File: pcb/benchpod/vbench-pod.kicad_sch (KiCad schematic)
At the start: 117 parts, among them J1 PZ254V-12-22P, SW1 TS-1088-AR02016, SW2 TS-1088-AR02016, U1 ICE40UP5K-SG48ITR, U10 TCAN1044VDRBRQ1, U2 W25Q64JVSSIQ, U24 SN74LVC2G66DCUR, U28 SRV05-4.TCT, U4 ESP32-C3-MINI-1-N4, U5 STM32H563ZIT6, U7 APS6404L-3SQR-ZR, U8 TPS2116DRLR, X1 SX3M48.000B10F20TNN, Y2 6pF ±10ppm SMD2016-4P Crystal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

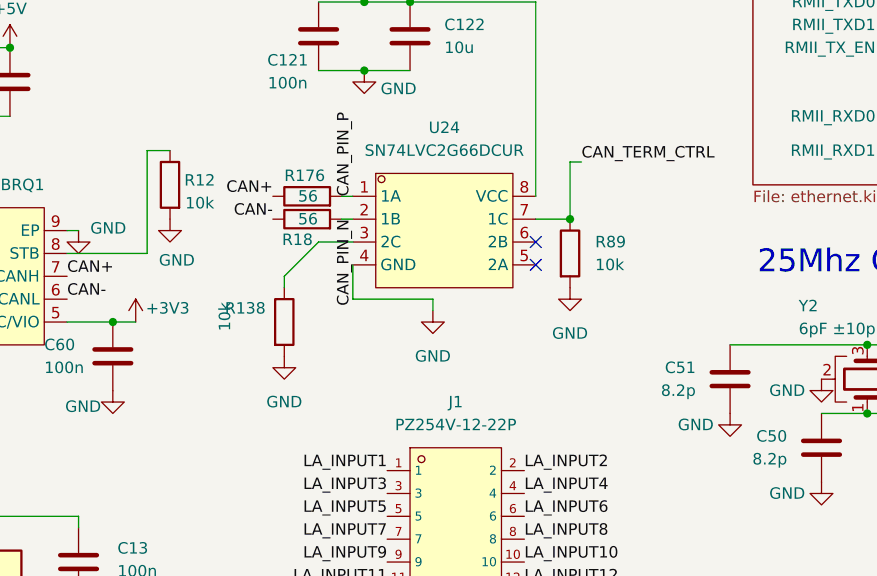
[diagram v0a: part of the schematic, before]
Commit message: CAN improvements, rerouting, final drc cleanup of routes
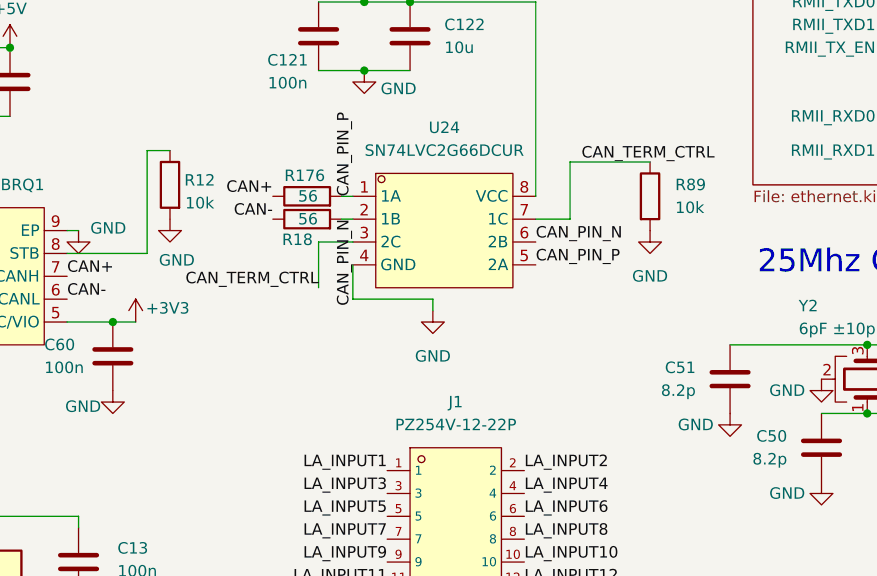
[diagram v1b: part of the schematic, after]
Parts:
- removed R138: 10k, Resistor_SMD:R_0402_1005Metric, symbol Device:R
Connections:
- net CAN_PIN_N: now also U24.6 (2B)
- net CAN_PIN_P: now also U24.5 (2A)
- net CAN_TERM_CTRL: now also U24.3 (2C)
- no-connect marks 62 -> 60
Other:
- moved on the sheet: R89

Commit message: fb changes, cc sensing, cleanups
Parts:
- FB2: footprint lcsc:L0603 -> lcsc_footprints:C85833_L0603; LCSC C1002 -> C85833
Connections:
- net CC_SENSE1: now reaches U5.26 (PC0)
- net CC_SENSE2: now reaches U5.28 (PC2)
- no-connect marks 60 -> 58
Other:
- sheet USB ports: added CC_SENSE1, CC_SENSE2; removed none
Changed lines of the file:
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@@
 	)
 	(no_connect
-		(at 330.2 116.84)
-	)
-	(no_connect
 		(at 330.2 83.82)
 	)
@@
 	)
 	(no_connect
-		(at 330.2 121.92)
-	)
-	(no_connect
 		(at 373.38 91.44)
 	)
@@
 		)
 	)
+	(label "CC_SENSE1"
+		(at 113.03 43.18 0)
+		(effects
+			(font
+				(size 1.27 1.27)
+			)
+			(justify left bottom)
+		)
+	)
 	(label "STM32_VDD"
 		(at 330.2 127 180)
@@
 		)
 	)
+	(label "CC_SENSE2"
+		(at 330.2 121.92 180)
+		(effects
+			(font
+				(size 1.27 1.27)
+			)
+			(justify right bottom)
+		)
+	)
 	(label "DAC_SCLK"
 		(at 123.19 78.74 0)
@@
 		)
 	)
+	(label "CC_SENSE1"
+		(at 330.2 116.84 180)
+		(effects
+			(font
+				(size 1.27 1.27)
+			)
+			(justify right bottom)
+		)
+	)
 	(label "HEADER1_5"
 		(at 270.51 257.81 180)
@@
 		)
 	)
+	(label "CC_SENSE2"
+		(at 113.03 46.99 0)
+		(effects
+			(font
+				(size 1.27 1.27)
+			)
+			(justify left bottom)
+		)
+	)
 	(label "FDCAN1_RX"
 		(at 373.38 129.54 0)
@@
 			)
 		)
-		(property "Footprint" "lcsc:L0603"
+		(property "Footprint" "lcsc_footprints:C85833_L0603"
 			(at 286.512 128.27 90)
 			(hide yes)
@@
 			)
 		)
-		(property "LCSC" "C1002"
+		(property "LCSC" "C85833"
 			(at 288.29 128.27 0)
 			(hide yes)
@@
 			(effects
 				(font
+					(size 1.27 1.27)
+				)
+				(justify right)
+			)
+		)
+		(pin "CC_SENSE1" input
+			(at 113.03 43.18 0)
+			(effects
+				(font
+					(size 1.27 1.27)
+				)
+				(justify right)
+			)
+		)
+		(pin "CC_SENSE2" input
+			(at 113.03 46.99 0)
+			(effects
+				(font

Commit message: digital and analog cleanup
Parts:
- FB2: LCSC Part C1002 -> (none)
- R176, R18: LCSC C25127 -> C3013179
- U5: value STM32H563ZIT6 -> STM32H563ZGT6; LCSC C6807803 -> C29271104; LCSC Part C6807803 -> C29271104; MPN STM32H563ZIT6 -> (none)
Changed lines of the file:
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@@
 			)
 		)
-		(property "Value" "STM32H563ZIT6"
+		(property "Value" "STM32H563ZGT6"
 			(at 351.79 48.26 0)
 			(show_name no)
@@
 			)
 		)
-		(property "MPN" "STM32H563ZIT6"
-			(at 353.06 248.92 0)
-			(hide yes)
-			(show_name no)
-			(do_not_autoplace no)
-			(effects
-				(font
-					(size 1.27 1.27)
-				)
-			)
-		)
-		(property "LCSC Part" "C6807803"
+		(property "LCSC Part" "C29271104"
 			(at 353.06 251.46 0)
 			(hide yes)
@@
 			)
 		)
-		(property "LCSC" "C6807803"
+		(property "LCSC" "C29271104"
 			(at 353.06 143.51 0)
 			(hide yes)
@@
 			)
 		)
-		(property "LCSC Part" "C1002"
-			(at 288.29 128.27 0)
-			(hide yes)
-			(show_name no)
-			(do_not_autoplace no)
-			(effects
-				(font
-					(size 1.27 1.27)
-				)
-			)
-		)
 		(property "Arrow Part Number" ""
 			(at 288.29 128.27 0)
@@
 			)
 		)
-		(property "LCSC" "C25127"
+		(property "LCSC" "C3013179"
 			(at 184.15 148.59 0)
 			(hide yes)
@@
 			)
 		)
-		(property "LCSC" "C25127"
+		(property "LCSC" "C3013179"
 			(at 184.15 146.05 0)
 			(hide yes)

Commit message: Benchpod v3.0.1 work (#1)
* bom replacements and footprint replacements for out of stock items

* replacements and fixes

* smaller fixes

* finalized v3r1

* finshunt work on digital (wip)
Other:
- sheet USB ports: added INA_SCL, INA_SDA; removed none
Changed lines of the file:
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@@
 		)
 	)
+	(label "I2C0_SCL"
+		(at 113.03 50.8 0)
+		(effects
+			(font
+				(size 1.27 1.27)
+			)
+			(justify left bottom)
+		)
+	)
 	(label "ICE_STM32_CS0"
 		(at 83.82 196.85 180)
@@
 		)
 	)
+	(label "I2C0_SDA"
+		(at 113.03 53.34 0)
+		(effects
+			(font
+				(size 1.27 1.27)
+			)
+			(justify left bottom)
+		)
+	)
 	(label "LA_INPUT8"
 		(at 208.28 184.15 0)
@@
 			(effects
 				(font
+					(size 1.27 1.27)
+				)
+				(justify right)
+			)
+		)
+		(pin "INA_SCL" input
+			(at 113.03 50.8 0)
+			(effects
+				(font
+					(size 1.27 1.27)
+				)
+				(justify right)
+			)
+		)
+		(pin "INA_SDA" input
+			(at 113.03 53.34 0)
+			(effects
+				(font
